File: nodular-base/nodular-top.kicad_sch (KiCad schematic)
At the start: 5 parts, among them J1 Conn_01x30_MountingPin

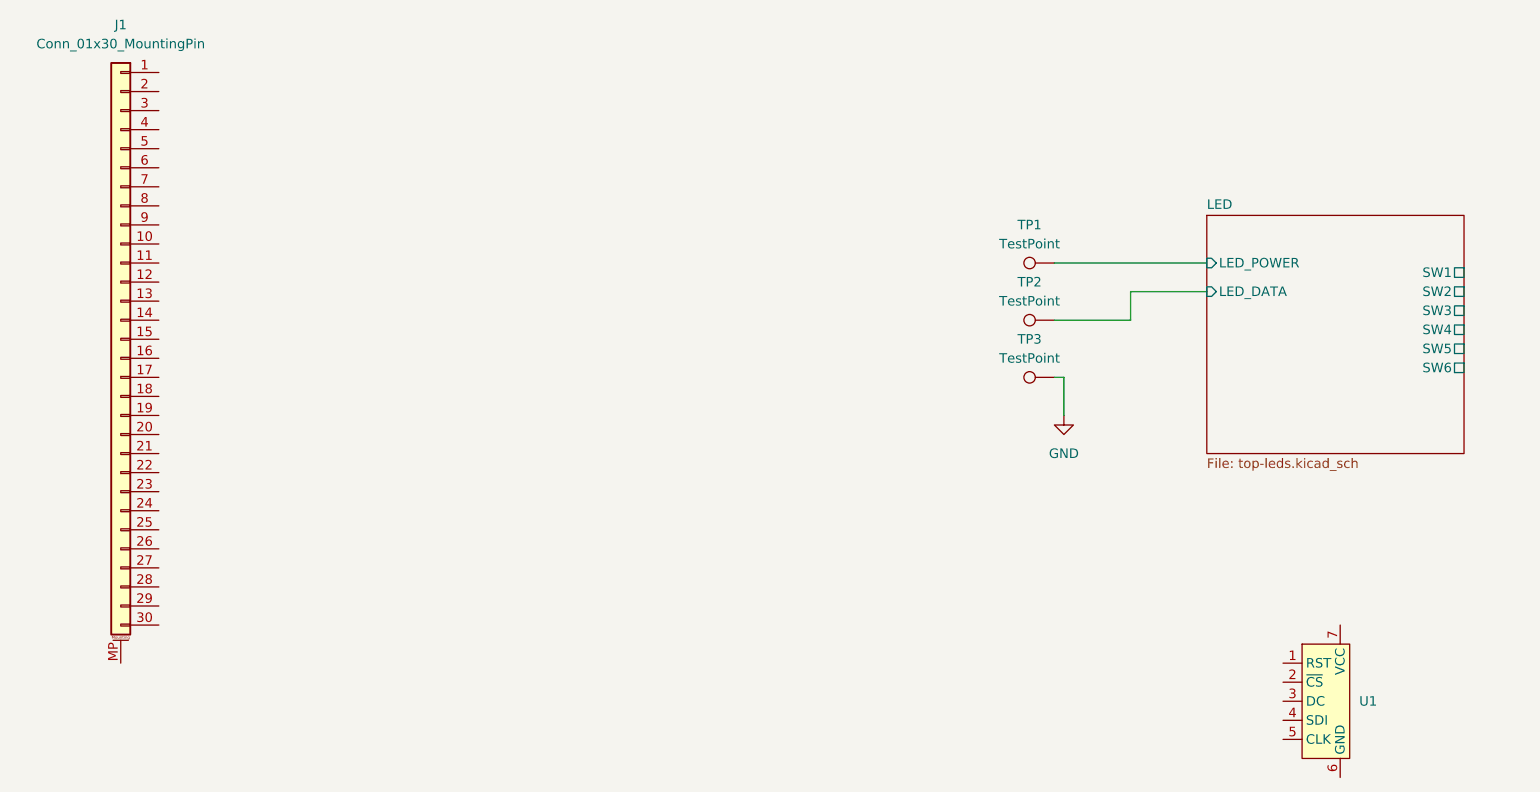
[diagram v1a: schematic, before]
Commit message: Add hole Add decoupling caps, pullups, and voltage dividers Set current limit on PMIC Determine battery attachment angle Update BOM and pinouts
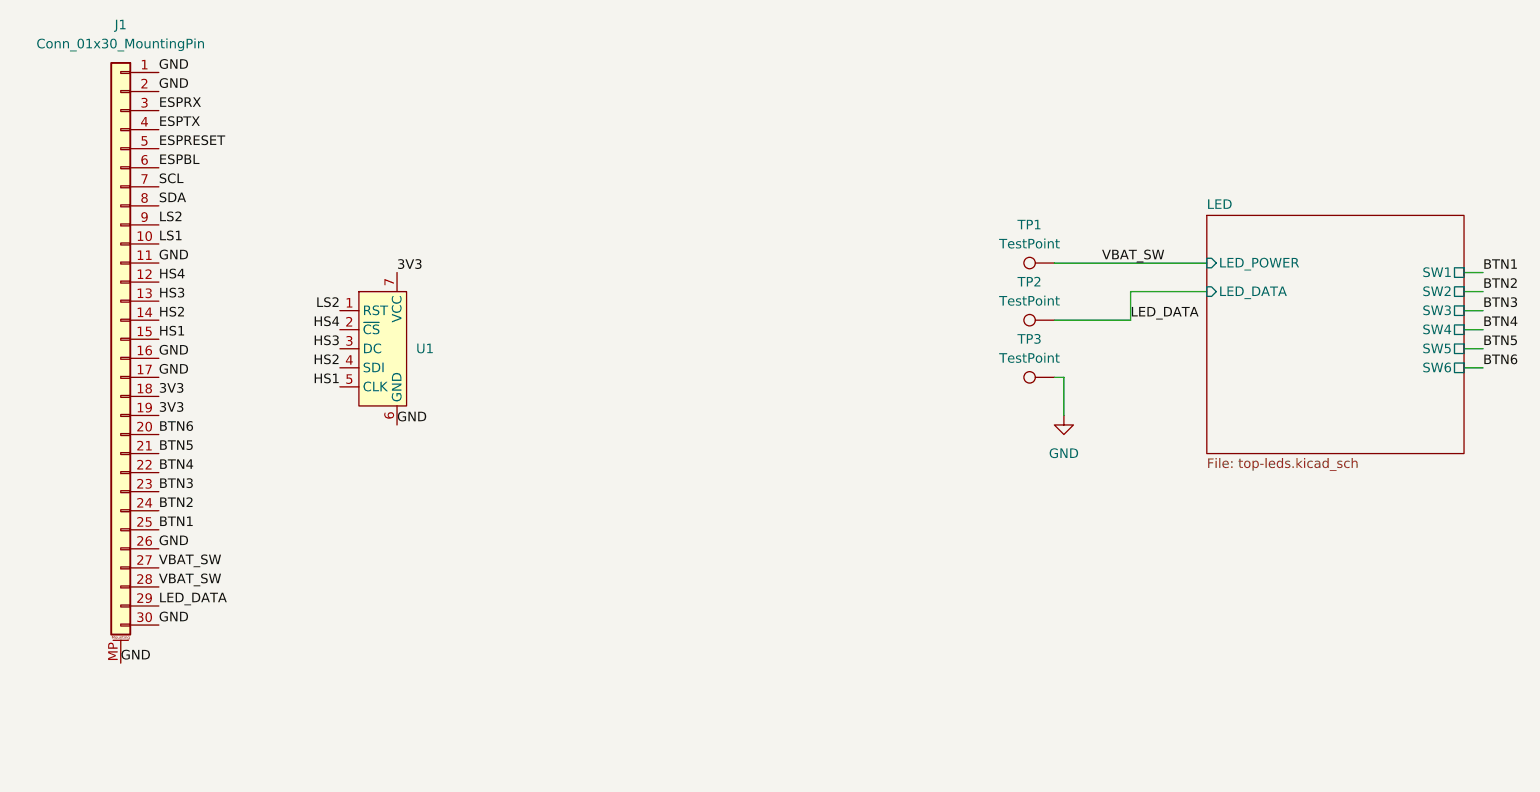
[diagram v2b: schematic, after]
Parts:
- J1: footprint Connector_FFC-FPC:Hirose_FH12-30S-0.5SH_1x30-1MP_P0.50mm_Horizontal -> nodular:Jushuo_AFC01-S30FCC-00_1x30-1MP_P0.50mm_Horizontal
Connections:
- net LED/LED_DATA is gone; now on net LED_DATA: TP2.1
- net LED/LED_POWER is gone; now on net VBAT_SW: TP1.1
- net GND: now also J1.1 (Pin_1), J1.11 (Pin_11), J1.16 (Pin_16), J1.17 (Pin_17), J1.2 (Pin_2), J1.26 (Pin_26), J1.30 (Pin_30), J1.MP (MountPin), U1.6 (GND)
- net LS2: now reaches U1.1 (RST)
- net LS2: now also J1.9 (Pin_9)
- net HS4: now reaches U1.2 (~{CS})
- net HS4: now also J1.12 (Pin_12)
- net HS3: now reaches U1.3 (DC)
- net HS3: now also J1.13 (Pin_13)
- net HS2: now reaches U1.4 (SDI)
- net HS2: now also J1.14 (Pin_14)
- net HS1: now reaches U1.5 (CLK)
- net HS1: now also J1.15 (Pin_15)
- net 3V3: now reaches U1.7 (VCC)
- net 3V3: now also J1.18 (Pin_18), J1.19 (Pin_19)
- net LS1: now reaches J1.10 (Pin_10)
- net BTN6: now reaches J1.20 (Pin_20)
- net BTN5: now reaches J1.21 (Pin_21)
- net BTN4: now reaches J1.22 (Pin_22)
- net BTN3: now reaches J1.23 (Pin_23)
- net BTN2: now reaches J1.24 (Pin_24)
- net BTN1: now reaches J1.25 (Pin_25)
- net VBAT_SW: now reaches J1.27 (Pin_27)
- net VBAT_SW: now also J1.28 (Pin_28)
- net LED_DATA: now reaches J1.29 (Pin_29)
- net ESPRX: now reaches J1.3 (Pin_3)
- net ESPTX: now reaches J1.4 (Pin_4)
- net ESPRESET: now reaches J1.5 (Pin_5)
- net ESPBL: now reaches J1.6 (Pin_6)
- net SCL: now reaches J1.7 (Pin_7)
- net SDA: now reaches J1.8 (Pin_8)
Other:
- moved on the sheet: U1
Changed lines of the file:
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@@
+    (stroke (width 0) (type default))
+  )
+  (wire (pts (xy 229.87 85.09) (xy 232.41 85.09))
+    (stroke (width 0) (type default))
+  )
+  (wire (pts (xy 229.87 87.63) (xy 232.41 87.63))
     (stroke (width 0) (type default))
   )
@@
     (stroke (width 0) (type default))
   )
+  (wire (pts (xy 229.87 82.55) (xy 232.41 82.55))
+    (stroke (width 0) (type default))
+  )
   (wire (pts (xy 175.26 88.9) (xy 176.53 88.9))
     (stroke (width 0) (type default))
   )
+  (wire (pts (xy 229.87 77.47) (xy 232.41 77.47))
+    (stroke (width 0) (type default))
+  )
   (wire (pts (xy 175.26 73.66) (xy 195.58 73.66))
     (stroke (width 0) (type default))
@@
     (stroke (width 0) (type default))
   )
+  (wire (pts (xy 229.87 80.01) (xy 232.41 80.01))
+    (stroke (width 0) (type default))
+  )
+  (wire (pts (xy 229.87 74.93) (xy 232.41 74.93))
+    (stroke (width 0) (type default))
+  )
   (wire (pts (xy 176.53 88.9) (xy 176.53 93.98))
     (stroke (width 0) (type default))
   )
+  (label "ESPBL" (at 55.88 60.96 0) (fields_autoplaced)
+    (effects (font (size 1.27 1.27)) (justify left bottom))
+  )
+  (label "LS2" (at 80.01 80.01 180) (fields_autoplaced)
+    (effects (font (size 1.27 1.27)) (justify right bottom))
+  )
+  (label "BTN5" (at 55.88 99.06 0) (fields_autoplaced)
+    (effects (font (size 1.27 1.27)) (justify left bottom))
+  )
+  (label "GND" (at 55.88 48.26 0) (fields_autoplaced)
+    (effects (font (size 1.27 1.27)) (justify left bottom))
+  )
+  (label "GND" (at 55.88 111.76 0) (fields_autoplaced)
+    (effects (font (size 1.27 1.27)) (justify left bottom))
+  )
+  (label "HS1" (at 80.01 90.17 180) (fields_autoplaced)
+    (effects (font (size 1.27 1.27)) (justify right bottom))
+  )
+  (label "HS2" (at 80.01 87.63 180) (fields_autoplaced)
+    (effects (font (size 1.27 1.27)) (justify right bottom))
+  )
+  (label "BTN6" (at 55.88 96.52 0) (fields_autoplaced)
+    (effects (font (size 1.27 1.27)) (justify left bottom))
+  )
+  (label "BTN3" (at 232.41 80.01 0) (fields_autoplaced)
+    (effects (font (size 1.27 1.27)) (justify left bottom))
+  )
+  (label "LS1" (at 55.88 71.12 0) (fields_autoplaced)
+    (effects (font (size 1.27 1.27)) (justify left bottom))
+  )
+  (label "ESPRESET" (at 55.88 58.42 0) (fields_autoplaced)
+    (effects (font (size 1.27 1.27)) (justify left bottom))
+  )
+  (label "HS2" (at 55.88 81.28 0) (fields_autoplaced)
+    (effects (font (size 1.27 1.27)) (justify left bottom))
+  )
+  (label "GND" (at 55.88 88.9 0) (fields_autoplaced)
+    (effects (font (size 1.27 1.27)) (justify left bottom))
+  )
+  (label "LED_DATA" (at 55.88 119.38 0) (fields_autoplaced)
+    (effects (font (size 1.27 1.27)) (justify left bottom))
+  )
+  (label "HS1" (at 55.88 83.82 0) (fields_autoplaced)
+    (effects (font (size 1.27 1.27)) (justify left bottom))
+  )
+  (label "BTN1" (at 55.88 109.22 0) (fields_autoplaced)
+    (effects (font (size 1.27 1.27)) (justify left bottom))
+  )
+  (label "SDA" (at 55.88 66.04 0) (fields_autoplaced)
+    (effects (font (size 1.27 1.27)) (justify left bottom))
+  )
+  (label "GND" (at 50.8 127 0) (fields_autoplaced)
+    (effects (font (size 1.27 1.27)) (justify left bottom))
+  )
+  (label "VBAT_SW" (at 55.88 116.84 0) (fields_autoplaced)
+    (effects (font (size 1.27 1.27)) (justify left bottom))
+  )
+  (label "HS3" (at 55.88 78.74 0) (fields_autoplaced)
+    (effects (font (size 1.27 1.27)) (justify left bottom))
+  )
+  (label "SCL" (at 55.88 63.5 0) (fields_autoplaced)
+    (effects (font (size 1.27 1.27)) (justify left bottom))
+  )
+  (label "LED_DATA" (at 185.42 81.28 0) (fields_autoplaced)
+    (effects (font (size 1.27 1.27)) (justify left bottom))
+  )
+  (label "GND" (at 55.88 86.36 0) (fields_autoplaced)
+    (effects (font (size 1.27 1.27)) (justify left bottom))
+  )
+  (label "BTN5" (at 232.41 85.09 0) (fields_autoplaced)
+    (effects (font (size 1.27 1.27)) (justify left bottom))
+  )
+  (label "HS3" (at 80.01 85.09 180) (fields_autoplaced)
+    (effects (font (size 1.27 1.27)) (justify right bottom))
+  )
+  (label "BTN3" (at 55.88 104.14 0) (fields_autoplaced)
+    (effects (font (size 1.27 1.27)) (justify left bottom))
+  )
+  (label "BTN2" (at 232.41 77.47 0) (fields_autoplaced)
+    (effects (font (size 1.27 1.27)) (justify left bottom))
+  )
+  (label "3V3" (at 55.88 91.44 0) (fields_autoplaced)
+    (effects (font (size 1.27 1.27)) (justify left bottom))
+  )
+  (label "GND" (at 55.88 73.66 0) (fields_autoplaced)
+    (effects (font (size 1.27 1.27)) (justify left bottom))
+  )
+  (label "ESPRX" (at 55.88 53.34 0) (fields_autoplaced)
+    (effects (font (size 1.27 1.27)) (justify left bottom))
+  )
+  (label "3V3" (at 55.88 93.98 0) (fields_autoplaced)
+    (effects (font (size 1.27 1.27)) (justify left bottom))
+  )
+  (label "BTN6" (at 232.41 87.63 0) (fields_autoplaced)
+    (effects (font (size 1.27 1.27)) (justify left bottom))
+  )
+  (label "BTN2" (at 55.88 106.68 0) (fields_autoplaced)
+    (effects (font (size 1.27 1.27)) (justify left bottom))
+  )
+  (label "BTN1" (at 232.41 74.93 0) (fields_autoplaced)
+    (effects (font (size 1.27 1.27)) (justify left bottom))
+  )
+  (label "3V3" (at 87.63 74.93 0) (fields_autoplaced)
+    (effects (font (size 1.27 1.27)) (justify left bottom))
+  )
+  (label "VBAT_SW" (at 181.61 73.66 0) (fields_autoplaced)
+    (effects (font (size 1.27 1.27)) (justify left bottom))
+  )
+  (label "GND" (at 55.88 121.92 0) (fields_autoplaced)
+    (effects (font (size 1.27 1.27)) (justify left bottom))
+  )
+  (label "GND" (at 87.63 95.25 0) (fields_autoplaced)
+    (effects (font (size 1.27 1.27)) (justify left bottom))
+  )
+  (label "VBAT_SW" (at 55.88 114.3 0) (fields_autoplaced)
+    (effects (font (size 1.27 1.27)) (justify left bottom))
+  )
+  (label "BTN4" (at 55.88 101.6 0) (fields_autoplaced)
+    (effects (font (size 1.27 1.27)) (justify left bottom))
+  )
+  (label "HS4" (at 80.01 82.55 180) (fields_autoplaced)
+    (effects (font (size 1.27 1.27)) (justify right bottom))
+  )
+  (label "GND" (at 55.88 50.8 0) (fields_autoplaced)
+    (effects (font (size 1.27 1.27)) (justify left bottom))
+  )
+  (label "HS4" (at 55.88 76.2 0) (fields_autoplaced)
+    (effects (font (size 1.27 1.27)) (justify left bottom))
+  )
+  (label "LS2" (at 55.88 68.58 0) (fields_autoplaced)
+    (effects (font (size 1.27 1.27)) (justify left bottom))
+  )
+  (label "BTN4" (at 232.41 82.55 0) (fields_autoplaced)
+    (effects (font (size 1.27 1.27)) (justify left bottom))
+  )
+  (label "ESPTX" (at 55.88 55.88 0) (fields_autoplaced)
+    (effects (font (size 1.27 1.27)) (justify left bottom))
+  )
   (symbol (lib_id "Connector:TestPoint") (at 175.26 88.9 90) (unit 1)
     (in_bom yes) (on_board yes) (dnp no) (fields_autoplaced)
@@
     )
   )
-  (symbol (lib_id "nodular:roundscreen") (at 213.36 132.08 0) (unit 1)
-    (in_bom yes) (on_board yes) (dnp no) (fields_autoplaced)
-    (property "Reference" "U1" (at 215.9 132.08 0)
+  (symbol (lib_id "nodular:roundscreen") (at 87.63 85.09 0) (unit 1)
+    (in_bom yes) (on_board yes) (dnp no) (fields_autoplaced)
+    (property "Reference" "U1" (at 90.17 85.09 0)
       (effects (font (size 1.27 1.27)) (justify left))
     )
-    (property "Value" "~" (at 213.36 132.08 0)
-      (effects (font (size 1.27 1.27)))
-    )
-    (property "Footprint" "nodular:PinHeader_1x07_P2.54mm_Vertical_LockPads" (at 213.36 132.08 0)
-      (effects (font (size 1.27 1.27)) hide)
-    )
-    (property "Datasheet" "" (at 213.36 132.08 0)
+    (property "Value" "~" (at 87.63 85.09 0)
+      (effects (font (size 1.27 1.27)))
+    )
+    (property "Footprint" "nodular:PinHeader_1x07_P2.54mm_Vertical_LockPads" (at 87.63 85.09 0)
+      (effects (font (size 1.27 1.27)) hide)
+    )
+    (property "Datasheet" "" (at 87.63 85.09 0)
       (effects (font (size 1.27 1.27)) hide)
     )
@@
       (effects (font (size 1.27 1.27)))
     )
-    (property "Footprint" "Connector_FFC-FPC:Hirose_FH12-30S-0.5SH_1x30-1MP_P0.50mm_Horizontal" (at 50.8 83.82 0)
-      (effects (font (size 1.27 1.27)) hide)
-    )
+    (property "Footprint" "nodular:Jushuo_AFC01-S30FCC-00_1x30-1MP_P0.50mm_Horizontal" (at 50.8 83.82 0)
+      (effects (font (size 1.27 1.27)) hide)
+    )

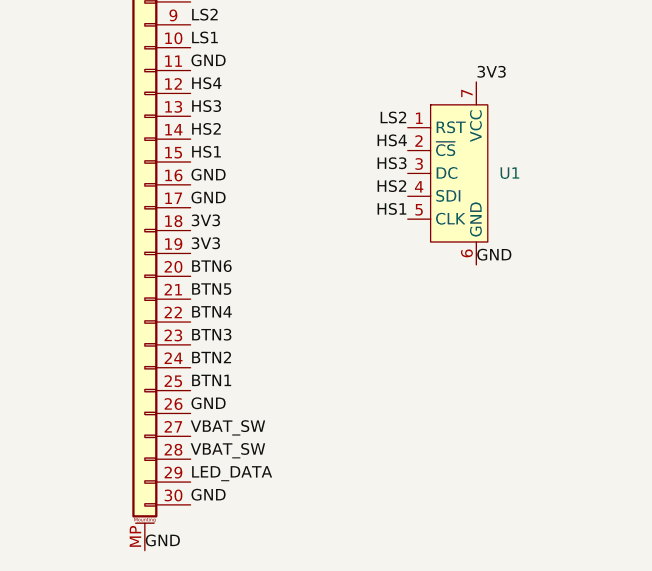
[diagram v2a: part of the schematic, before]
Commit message: Add 3d models and fix erc errors
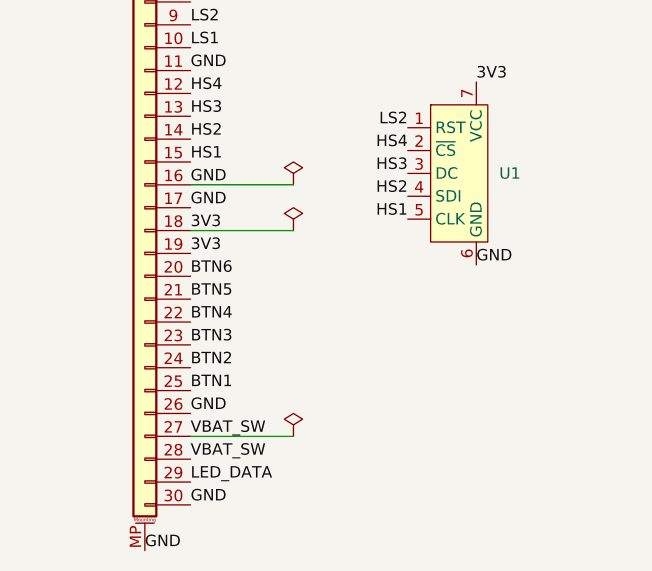
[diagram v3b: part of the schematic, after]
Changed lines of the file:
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@@
 (kicad_sch (version 20230121) (generator eeschema)
   (paper "A4")
+  (wire (pts (xy 55.88 86.36) (xy 67.31 86.36))
+    (stroke (width 0) (type default))
+  )
   (wire (pts (xy 185.42 77.47) (xy 185.42 81.28))
     (stroke (width 0) (type default))
@@
     (stroke (width 0) (type default))
   )
+  (wire (pts (xy 55.88 114.3) (xy 67.31 114.3))
+    (stroke (width 0) (type default))
+  )
   (wire (pts (xy 229.87 80.01) (xy 232.41 80.01))
     (stroke (width 0) (type default))
@@
   )
   (wire (pts (xy 176.53 88.9) (xy 176.53 93.98))
+    (stroke (width 0) (type default))
+  )
+  (wire (pts (xy 55.88 91.44) (xy 67.31 91.44))
     (stroke (width 0) (type default))
   )
@@
     (effects (font (size 1.27 1.27)) (justify left bottom))
   )
+  (symbol (lib_id "power:PWR_FLAG") (at 67.31 86.36 0) (unit 1)
+    (in_bom yes) (on_board yes) (dnp no) (fields_autoplaced)
+    (property "Reference" "#FLG01" (at 67.31 84.455 0)
+      (effects (font (size 1.27 1.27)) hide)
+    )
+    (property "Value" "PWR_FLAG" (at 67.31 81.28 0)
+      (effects (font (size 1.27 1.27)) hide)
+    )
+    (property "Footprint" "" (at 67.31 86.36 0)
+      (effects (font (size 1.27 1.27)) hide)
+    )
+    (property "Datasheet" "~" (at 67.31 86.36 0)
+      (effects (font (size 1.27 1.27)) hide)
+    )
+    (pin "1")
+    (instances
+      (project "nodular-top"
+        (path "/67223bb4-fb4b-4d28-a5c8-1b64a0b88fc4"
+          (reference "#FLG01") (unit 1)
+        )
+      )
+    )
+  )
   (symbol (lib_id "Connector:TestPoint") (at 175.26 88.9 90) (unit 1)
     (in_bom yes) (on_board yes) (dnp no) (fields_autoplaced)
@@
         (path "/67223bb4-fb4b-4d28-a5c8-1b64a0b88fc4"
           (reference "TP1") (unit 1)
+        )
+      )
+    )
+  )
+  (symbol (lib_id "power:PWR_FLAG") (at 67.31 114.3 0) (unit 1)
+    (in_bom yes) (on_board yes) (dnp no) (fields_autoplaced)
+    (property "Reference" "#FLG03" (at 67.31 112.395 0)
+      (effects (font (size 1.27 1.27)) hide)
+    )
+    (property "Value" "PWR_FLAG" (at 67.31 109.22 0)
+      (effects (font (size 1.27 1.27)) hide)
+    )
+    (property "Footprint" "" (at 67.31 114.3 0)
+      (effects (font (size 1.27 1.27)) hide)
+    )
+    (property "Datasheet" "~" (at 67.31 114.3 0)
+      (effects (font (size 1.27 1.27)) hide)
+    )
+    (pin "1")
+    (instances
+      (project "nodular-top"
+        (path "/67223bb4-fb4b-4d28-a5c8-1b64a0b88fc4"
+          (reference "#FLG03") (unit 1)
         )
       )
@@
         )
       )
+    )
+  )
+  (symbol (lib_id "power:PWR_FLAG") (at 67.31 91.44 0) (unit 1)
+    (in_bom yes) (on_board yes) (dnp no) (fields_autoplaced)
+    (property "Reference" "#FLG02" (at 67.31 89.535 0)
+      (effects (font (size 1.27 1.27)) hide)
+    )
+    (property "Value" "PWR_FLAG" (at 67.31 86.36 0)
+      (effects (font (size 1.27 1.27)) hide)
+    )
+    (property "Footprint" "" (at 67.31 91.44 0)
+      (effects (font (size 1.27 1.27)) hide)
+    )
+    (property "Datasheet" "~" (at 67.31 91.44 0)
+      (effects (font (size 1.27 1.27)) hide)
+    )
+    (pin "1")
+    (instances
+      (project "nodular-top"
+        (path "/67223bb4-fb4b-4d28-a5c8-1b64a0b88fc4"
+          (reference "#FLG02") (unit 1)
+        )
+      )
